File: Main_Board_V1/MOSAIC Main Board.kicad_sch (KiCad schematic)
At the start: 82 parts, among them J1 CONN E, J10 QWIIC_RIGHT_ANGLE, J11 Vertical Qwiic Connector, J12 CONN E, J13 CONN E, J14 35RAPC4BH3 CONN 3.5MM, J2 CONN E, J3 CONN E, J4 CONN HEADER VERT 10POS 1.27MM, J5 USB TYPE C R/A SMT 16PIN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

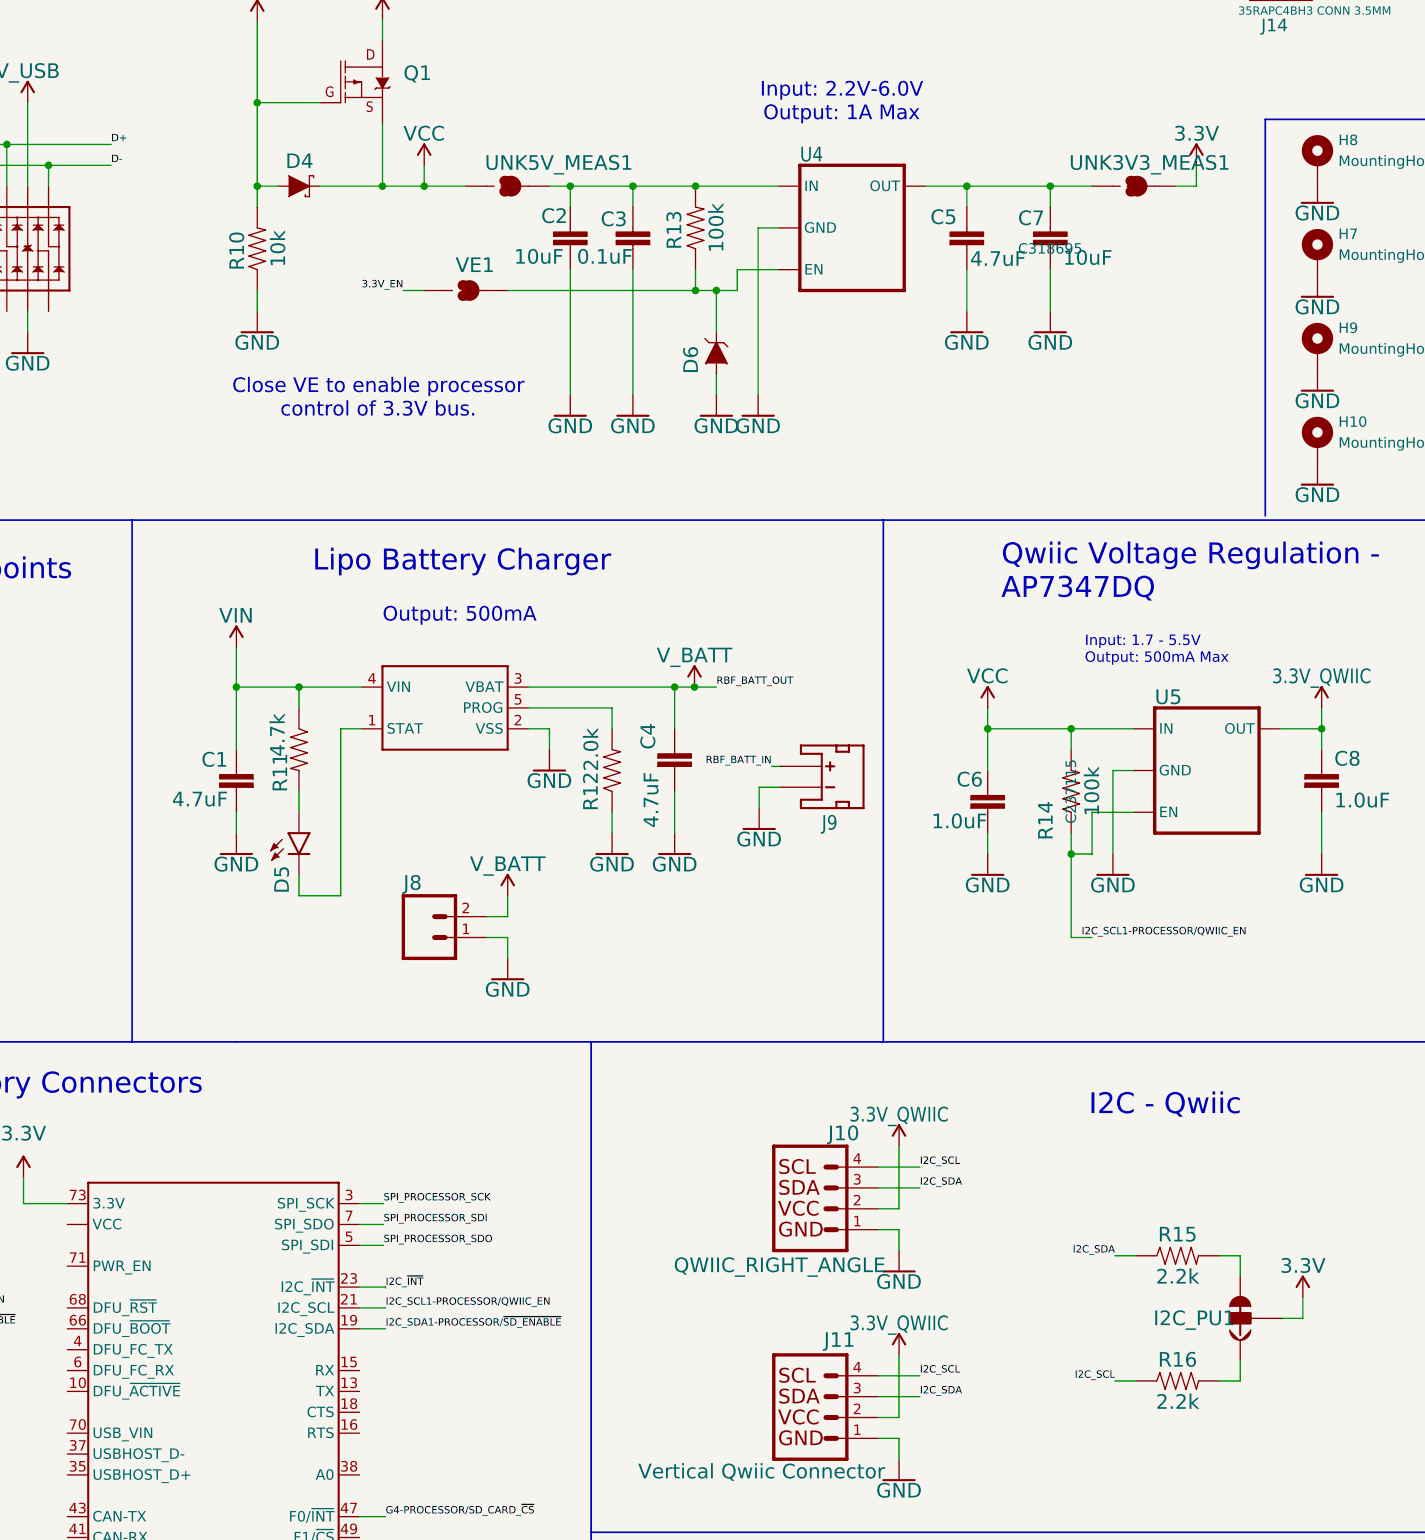
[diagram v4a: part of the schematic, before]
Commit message: add jlcpcb comp sources
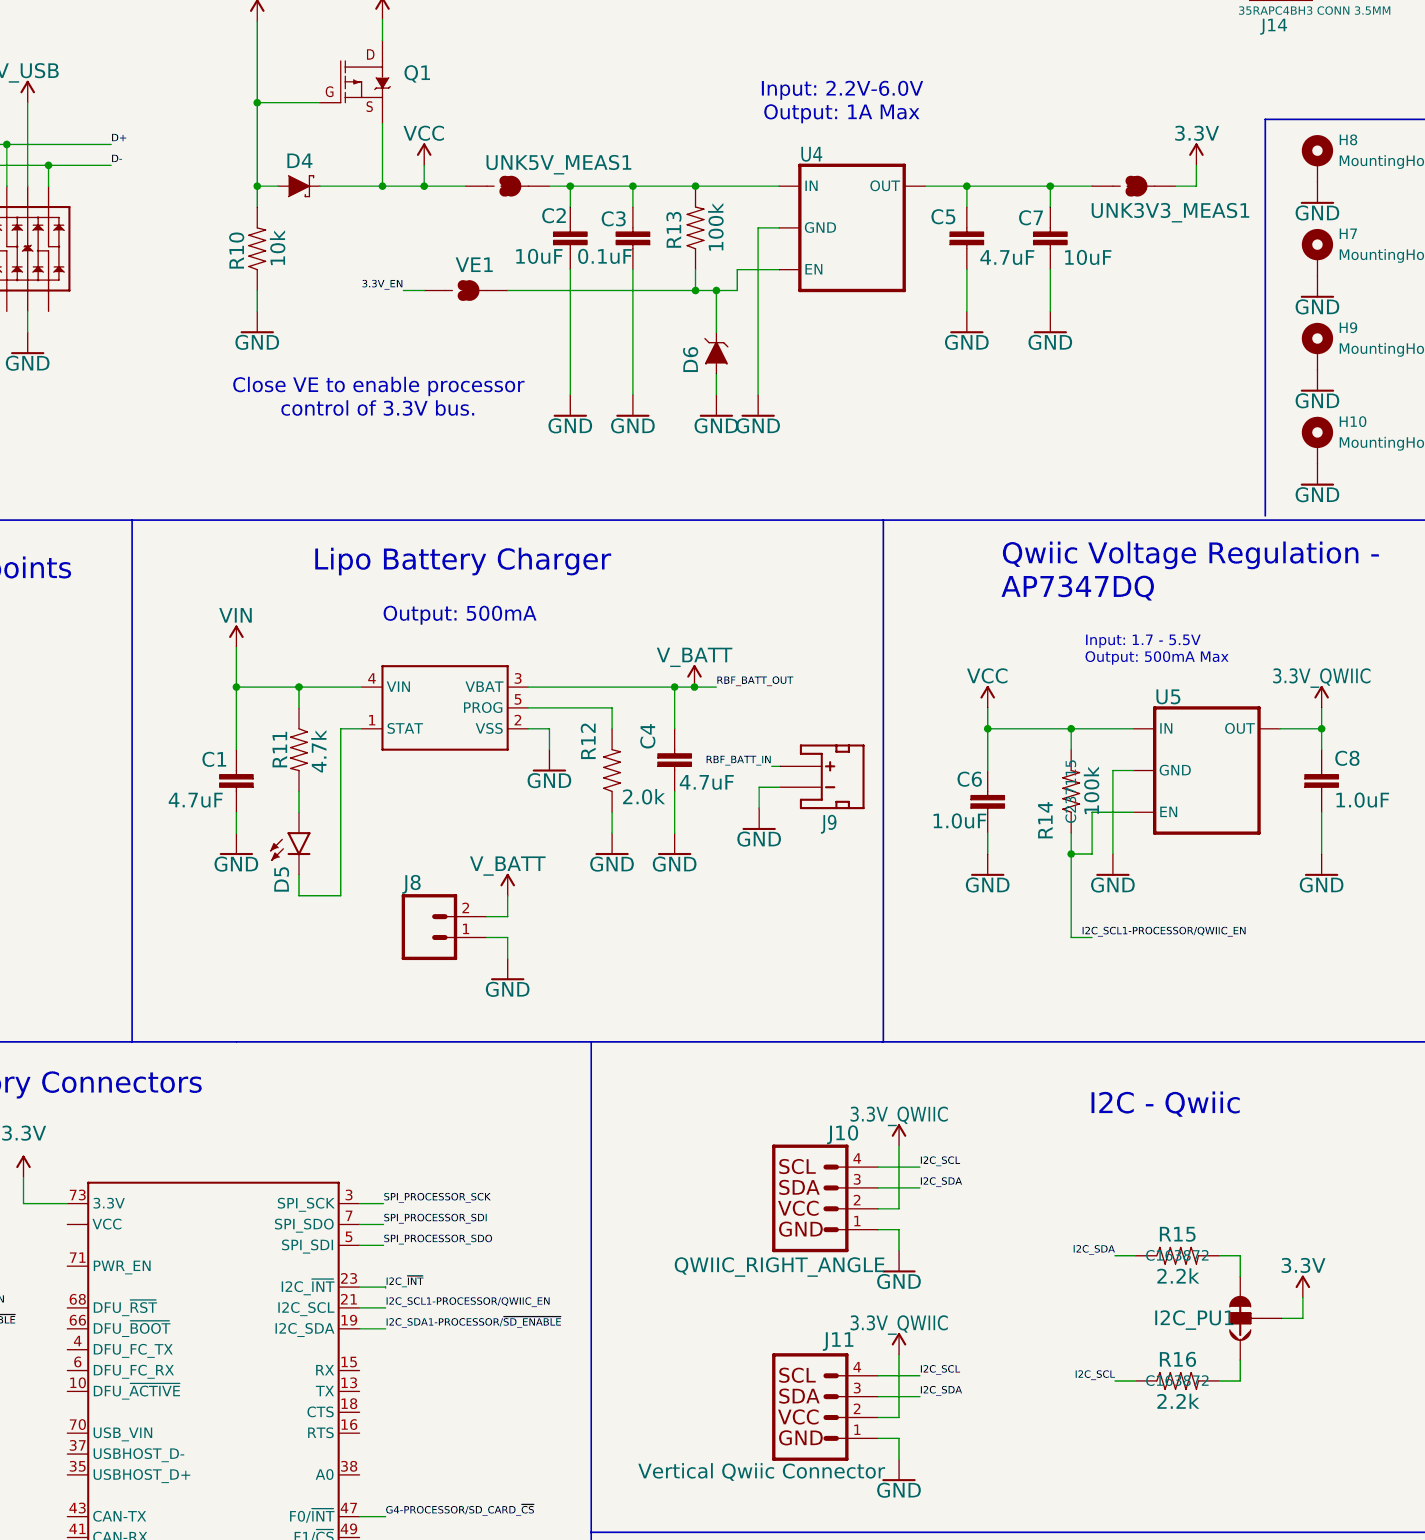
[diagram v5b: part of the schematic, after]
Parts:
- 3.3V1, GND1, H3, J14, J8, QWIIC_LED1, SWDIO2, UNK3V3_LED1, UNK3V3_MEAS1, UNK5V_LED1, VIN1, V_BATT1: now left out of the parts list
- C1, C4, C5: JLCPCB Part # (none) -> C1705; Source https://www.digikey.com/en/products/detail/samsung-electro-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 -> (none)
- D1: JLCPCB Part # (none) -> C125099; Source https://www.digikey.com/en/products/detail/liteon/LTST-C191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 -> (none)
- D2, D3: JLCPCB Part # (none) -> C125099; Source https://www.digikey.com/en/products/detail/w%C3%BCrth-elekt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 -> (none)
- D5: JLCPCB Part # (none) -> C125095; Source https://www.digikey.com/en/products/detail/liteon/LTST-C190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 -> (none)
- D6: JLCPCB Part # (none) -> C550557; Source https://www.mouser.com/ProductDetail/Diotec-Semiconductor/M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 -> (none)
- J9: Source https://www.mouser.com/ProductDetail/Adafruit/1769?qs=GURaw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 -> (none); now left out of the parts list
- R11: JLCPCB Part # (none) -> C4293273; Source https://www.digikey.com/en/products/detail/stackpole-electr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 -> (none)
- R12: JLCPCB Part # (none) -> C2076433; Source https://www.digikey.com/en/products/detail/bourns-inc/CR060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 -> (none)
- R15, R16, R3: JLCPCB Part # (none) -> C163872; Source https://www.digikey.com/en/products/detail/walsin-technolog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 -> (none)
- R4: JLCPCB Part # (none) -> C2484712; Source https://www.digikey.com/en/products/detail/stackpole-electr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 -> (none)
- R7: Field4 https://www.digikey.com/en/products/detail/stackpole-electr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 -> (none); JLCPCB Part # (none) -> C2484712
- U3: JLCPCB Part # (none) -> C424093; Source https://www.digikey.com/en/products/detail/microchip-techno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 -> (none)
- U4: JLCPCB Part # (none) -> C151007; Source https://www.digikey.com/en/products/detail/diodes-incorpora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 -> (none)

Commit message: added jlcpcb comp sources
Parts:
- C6, C8: JLCPCB Part # (none) -> C1592; Source https://www.digikey.com/en/products/detail/samsung-electro-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 -> (none)
- H1, H2, H4, H5, H6: Source https://www.digikey.com/en/products/detail/w%C3%BCrth-elekt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 -> (none)
- I2C_PU1: now left out of the parts list
- J10: value QWIIC_RIGHT_ANGLE -> Right Angle Qwiic Connector; JLCPCB Part # C295747 -> C145956
- J11: JLCPCB Part # (none) -> C160390; Source https://www.sparkfun.com/products/14417 -> (none)
- U5: JLCPCB Part # (none) -> C2891277; Source https://www.digikey.com/en/products/detail/diodes-incorpora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 -> (none)
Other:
- note added: "Input: 1.7 - 6V Output: 500mA Max, Fixed 3.3V"
- note added: "Qwiic Voltage Regulation - XC6503D331MR"
- note removed: "Input: 1.7 - 5.5V Output: 500mA Max"
- note removed: "Qwiic Voltage Regulation - AP7347DQ"
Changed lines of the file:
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@@
 		)
 	)
-	(text "Input: 1.7 - 5.5V\nOutput: 500mA Max"
+	(text "Input: 1.7 - 6V\nOutput: 500mA Max, Fixed 3.3V"
 		(exclude_from_sim no)
-		(at 407.289 119.761 0)
+		(at 397.764 118.11 0)
 		(effects
 			(font
@@
 		)
 	)
-	(text "Qwiic Voltage Regulation - \nAP7347DQ"
+	(text "Qwiic Voltage Regulation - \nXC6503D331MR"
 		(exclude_from_sim no)
 		(at 397.129 112.014 0)
@@
 					(size 1.27 1.27)
 				)
-			)
-		)
-		(property "Source" "https://www.digikey.com/en/products/detail/w%C3%BCrth-elektronik/9774025151R/5320621"
-			(at 189.738 282.448 0)
-			(effects
-				(font
-					(size 1.27 1.27)
-				)
 				(hide yes)
 			)
@@
 		(unit 1)
 		(exclude_from_sim no)
-		(in_bom yes)
+		(in_bom no)
 		(on_board yes)
 		(dnp no)
 		(property "Reference" "I2C_PU1"
-			(at 420.624 199.263 0)
+			(at 418.592 199.39 0)
 			(effects
 				(font
@@
 					(size 1.778 1.778)
 				)
-				(hide yes)
 			)
 		)
@@
 					(size 1.27 1.27)
 				)
+				(hide yes)
 			)
 		)
@@
 					(size 1.27 1.27)
 				)
-			)
-		)
-		(property "Source" "https://www.digikey.com/en/products/detail/w%C3%BCrth-elektronik/9774025151R/5320621"
-			(at 192.278 282.448 0)
-			(effects
-				(font
-					(size 1.27 1.27)
-				)
 				(hide yes)
 			)
@@
 		(dnp no)
 		(property "Reference" "R14"
-			(at 403.606 138.684 0)
+			(at 404.114 135.128 0)
 			(effects
 				(font
@@
 		)
 		(property "JLCPCB Part #" "C237115"
-			(at 405.638 135.128 0)
+			(at 403.098 133.858 0)
 			(effects
 				(font
 					(size 1.27 1.27)
 				)
+				(hide yes)
 			)
 		)
@@
 					(size 1.27 1.27)
 				)
-			)
-		)
-		(property "Source" "https://www.digikey.com/en/products/detail/w%C3%BCrth-elektronik/9774025151R/5320621"
-			(at 194.818 282.448 0)
-			(effects
-				(font
-					(size 1.27 1.27)
-				)
 				(hide yes)
 			)
@@
 		)
 		(property "Value" "Vertical Qwiic Connector"
-			(at 352.933 218.948 0)
+			(at 351.536 222.25 0)
 			(effects
 				(font
 					(size 1.778 1.778)
 				)
-				(justify left bottom)
+				(justify left top)
 			)
 		)
@@
 			)
 		)
-		(property "Datasheet" "https://cdn.sparkfun.com/assets/parts/1/2/2/8/9/Qwiic_Connector_Datasheet.pdf"
+		(property "Datasheet" "https://jlcpcb.com/api/file/downloadByFileSystemAccessId/8588897884003569664"
 			(at 374.523 211.328 0)
 			(effects
@@
 			)
 		)
-		(property "Description" ""
+		(property "Description" "https://jlcpcb.com/partdetail/Jst-BM04B_SRSS_TB_LF_SN/C160390"
 			(at 374.523 211.328 0)
 			(effects
@@
 					(size 1.27 1.27)
 				)
+				(hide yes)
 			)
 		)
-		(property "Source" "https://www.sparkfun.com/products/14417"
+		(property "JLCPCB Part #" "C160390"
 			(at 374.523 211.328 0)
 			(effects
@@
 					(size 1.27 1.27)
 				)
-			)
-		)
-		(property "Source" "https://www.digikey.com/en/products/detail/w%C3%BCrth-elektronik/9774025151R/5320621"
-			(at 328.549 240.03 0)
-			(effects
-				(font
-					(size 1.27 1.27)
-				)
 				(hide yes)
 			)
@@
 		)
 		(property "JLCPCB Part #" "C163872"
-			(at 418.592 191.643 0)
+			(at 419.354 186.944 0)
 			(effects
 				(font
 					(size 1.27 1.27)
 				)
+				(hide yes)
 			)
 		)
@@
 		)
 		(property "JLCPCB Part #" "C237115"
-			(at 234.315 272.288 0)
+			(at 243.078 266.954 0)
 			(effects
 				(font
 					(size 1.27 1.27)
 				)
+				(hide yes)
 			)
 		)
@@
 			)
 		)
-		(property "Datasheet" "https://www.diodes.com/assets/Datasheets/AP7347DQ.pdf"
+		(property "Datasheet" "https://jlcpcb.com/api/file/downloadByFileSystemAccessId/8590196445028003840"
 			(at 423.418 132.588 0)
 			(effects
@@
 			)
 		)
-		(property "Description" ""
+		(property "Description" "https://jlcpcb.com/partdetail/TorexSemicon-XC6503D331MRG/C2891277"
 			(at 423.418 132.588 0)
 			(effects
@@
 					(size 1.27 1.27)
 				)
+				(hide yes)
 			)
 		)
-		(property "Source" "https://www.digikey.com/en/products/detail/diodes-incorporated/AP7347DQ-33W5-7/15516981"
+		(property "JLCPCB Part #" "C2891277"
 			(at 423.418 132.588 0)
 			(effects
@@
 					(size 1.27 1.27)
 				)
-			)
-		)
-		(property "Source" "https://www.digikey.com/en/products/detail/w%C3%BCrth-elektronik/9774025151R/5320621"
-			(at 335.788 240.03 0)
-			(effects
-				(font
-					(size 1.27 1.27)
-				)
 				(hide yes)
 			)
@@
 		)
 		(property "Value" "1.0uF"
-			(at 437.642 137.287 0)
+			(at 437.642 137.668 0)
 			(effects
 				(font
@@
 			)
 		)
-		(property "Datasheet" "https://mm.digikey.com/Volume0/opasdata/d220001/medias/docus/609/CL10A105KO8NNNC_Spec.pdf"
+		(property "Datasheet" "https://jlcpcb.com/api/file/downloadByFileSystemAccessId/8586178147360378880"
 			(at 436.118 135.128 0)
 			(effects
@@
 			)
 		)
-		(property "Description" ""
+		(property "Description" "https://jlcpcb.com/partdetail/1944-CL10A105KO8NNNC/C1592"
 			(at 436.118 135.128 0)
 			(effects
@@
 					(size 1.27 1.27)
 				)
+				(hide yes)
 			)
 		)
-		(property "Source" "https://www.digikey.com/en/products/detail/samsung-electro-mechanics/CL10A105KO8NNNC/3886692"
+		(property "JLCPCB Part #" "C1592"
 			(at 436.118 135.128 0)
 			(effects
@@
 		)
 		(property "JLCPCB Part #" "C163872"
-			(at 418.592 206.883 0)
+			(at 410.464 211.582 0)
 			(effects
 				(font
 					(size 1.27 1.27)
 				)
+				(hide yes)
 			)
 		)
@@
 		)
 		(property "JLCPCB Part #" "C237115"
-			(at 226.695 272.288 0)
+			(at 219.964 272.034 0)
 			(effects
 				(font
 					(size 1.27 1.27)
 				)
+				(hide yes)
 			)
 		)
@@
 			)
 		)
-		(property "Value" "QWIIC_RIGHT_ANGLE"
-			(at 357.251 191.77 0)
+		(property "Value" "Right Angle Qwiic Connector"
+			(at 350.266 170.688 0)
 			(effects
 				(font
@@
 			)
 		)
-		(property "Datasheet" "https://jlcpcb.com/api/file/downloadByFileSystemAccessId/8587740317575483392"
+		(property "Datasheet" "https://jlcpcb.com/api/file/downloadByFileSystemAccessId/8588895674171052032"
 			(at 374.523 185.928 0)
 			(effects
@@
 			)
 		)
-		(property "Description" "https://jlcpcb.com/partdetail/Jst-S2B_PH_SM4_TB_LF_SN/C295747"
+		(property "Description" "https://jlcpcb.com/partdetail/C145956"
 			(at 374.523 185.928 0)
 			(effects
@@
 			)
 		)
-		(property "JLCPCB Part #" "C295747"
+		(property "JLCPCB Part #" "C145956"
 			(at 374.523 185.928 0)
 			(effects
@@
 		)
 		(property "Value" "1.0uF"
-			(at 388.62 139.827 0)
+			(at 387.096 139.954 0)
 			(effects
 				(font
@@
 			)
 		)
-		(property "Datasheet" "https://mm.digikey.com/Volume0/opasdata/d220001/medias/docus/609/CL10A105KO8NNNC_Spec.pdf"
+		(property "Datasheet" "https://jlcpcb.com/api/file/downloadByFileSystemAccessId/8586178147360378880"
 			(at 395.478 137.668 0)
 			(effects
@@
 			)
 		)
-		(property "Description" ""
+		(property "Description" "https://jlcpcb.com/partdetail/1944-CL10A105KO8NNNC/C1592"
 			(at 395.478 137.668 0)
 			(effects
@@
 					(size 1.27 1.27)
 				)
+				(hide yes)
 			)
 		)
-		(property "Source" "https://www.digikey.com/en/products/detail/samsung-electro-mechanics/CL10A105KO8NNNC/3886692"
+		(property "JLCPCB Part #" "C1592"
 			(at 395.478 137.668 0)
 			(effects
